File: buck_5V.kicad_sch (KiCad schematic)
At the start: 15 parts, among them U3 TPS566238PRQFR

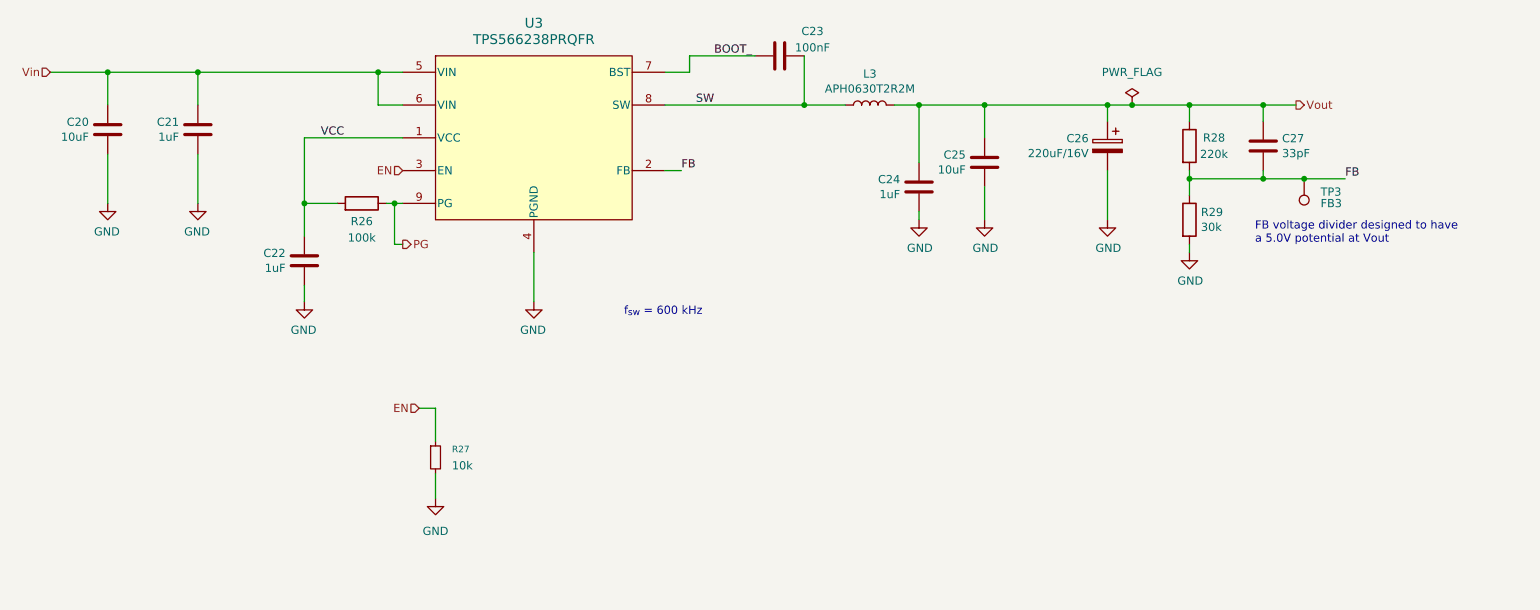
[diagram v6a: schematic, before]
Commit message: Update the design to a stackable one
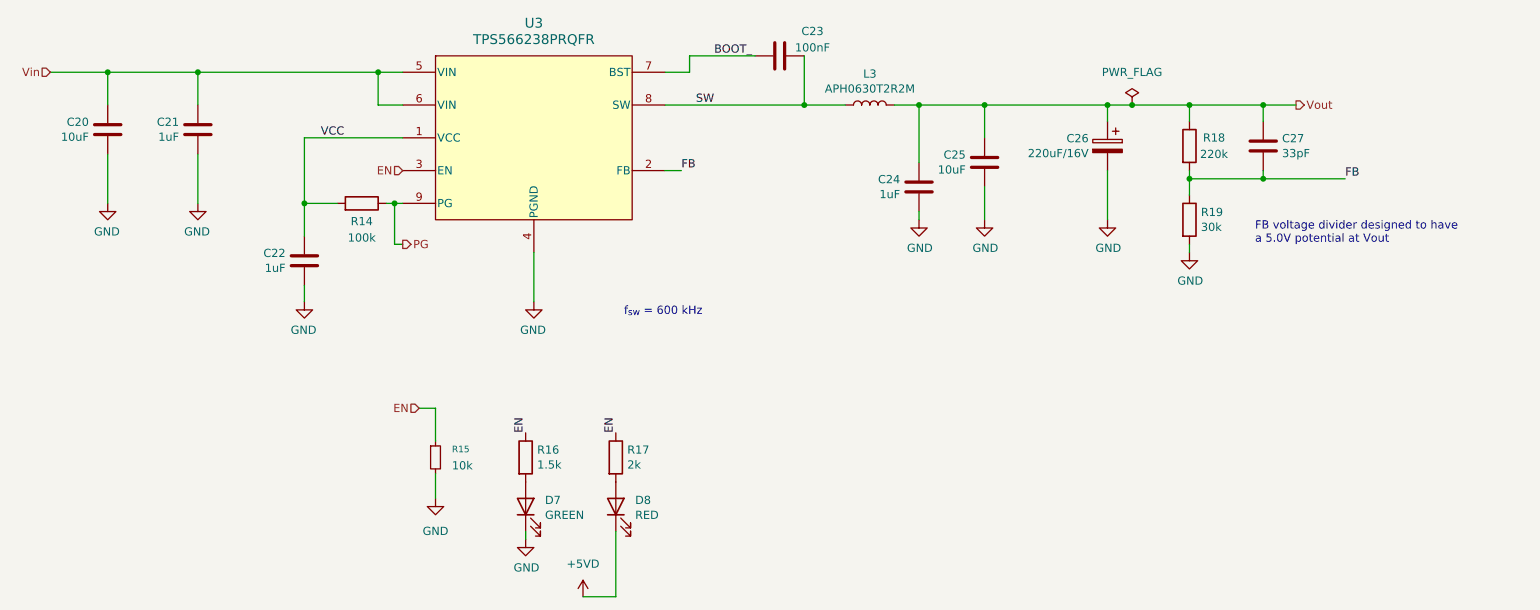
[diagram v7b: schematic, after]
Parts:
- removed TP3: FB3, TestPoint:TestPoint_Pad_D1.0mm, symbol Connector:TestPoint
- added D7: GREEN, LED_SMD:LED_0603_1608Metric, symbol Device:LED
- added D8: RED, LED_SMD:LED_0603_1608Metric, symbol Device:LED
- added R16: 1.5k, Resistor_SMD:R_0603_1608Metric, symbol Device:R
- added R17: 2k, Resistor_SMD:R_0603_1608Metric, symbol Device:R
- renumbered R26 to R14, R27 to R15, R28 to R18, R29 to R19
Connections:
- net EN: now also R16.1, R17.1
- net GND: now also D7.1 (K)
- new net: D7.2 (A), R16.2
- new net: D8.2 (A), R17.2
- new net +5VD: D8.1 (K)
